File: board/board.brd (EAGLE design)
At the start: 49.6 x 37.9 mm, 17 parts

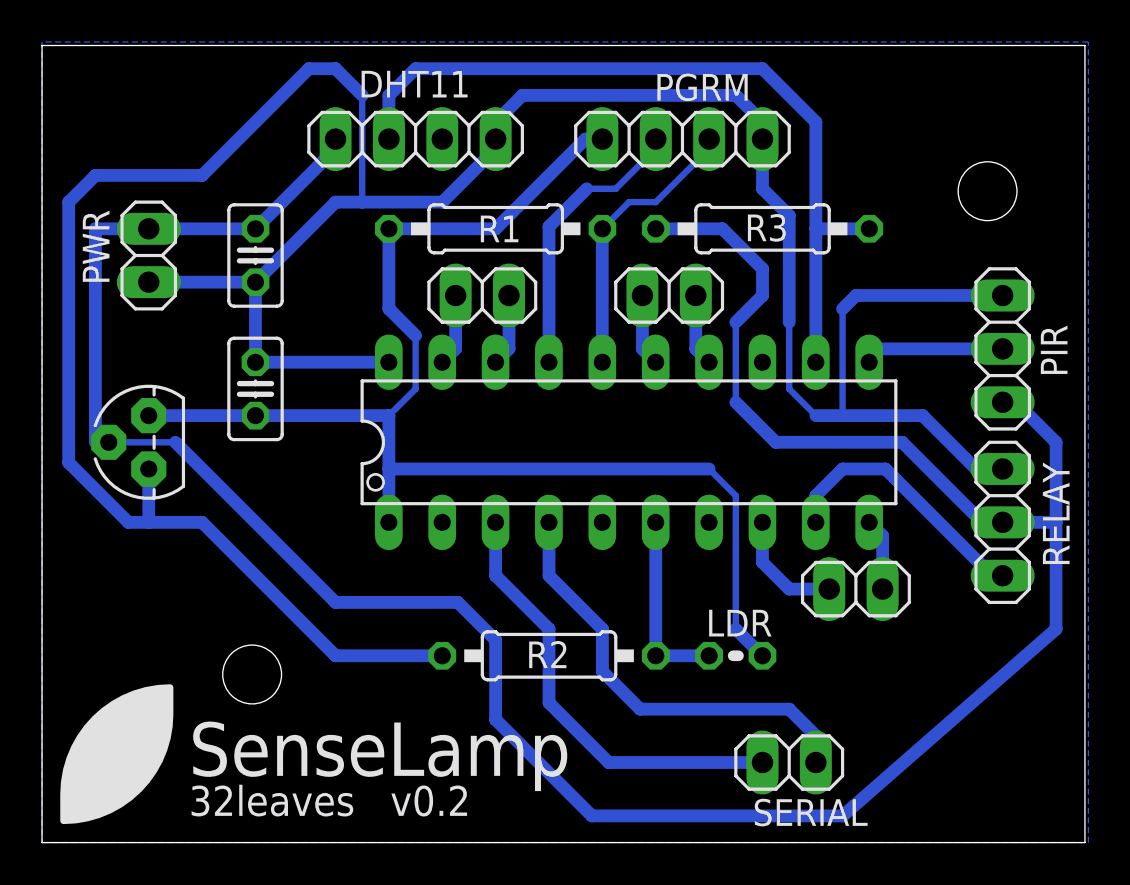
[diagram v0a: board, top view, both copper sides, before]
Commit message: fixed some space issues of the v0.1 board
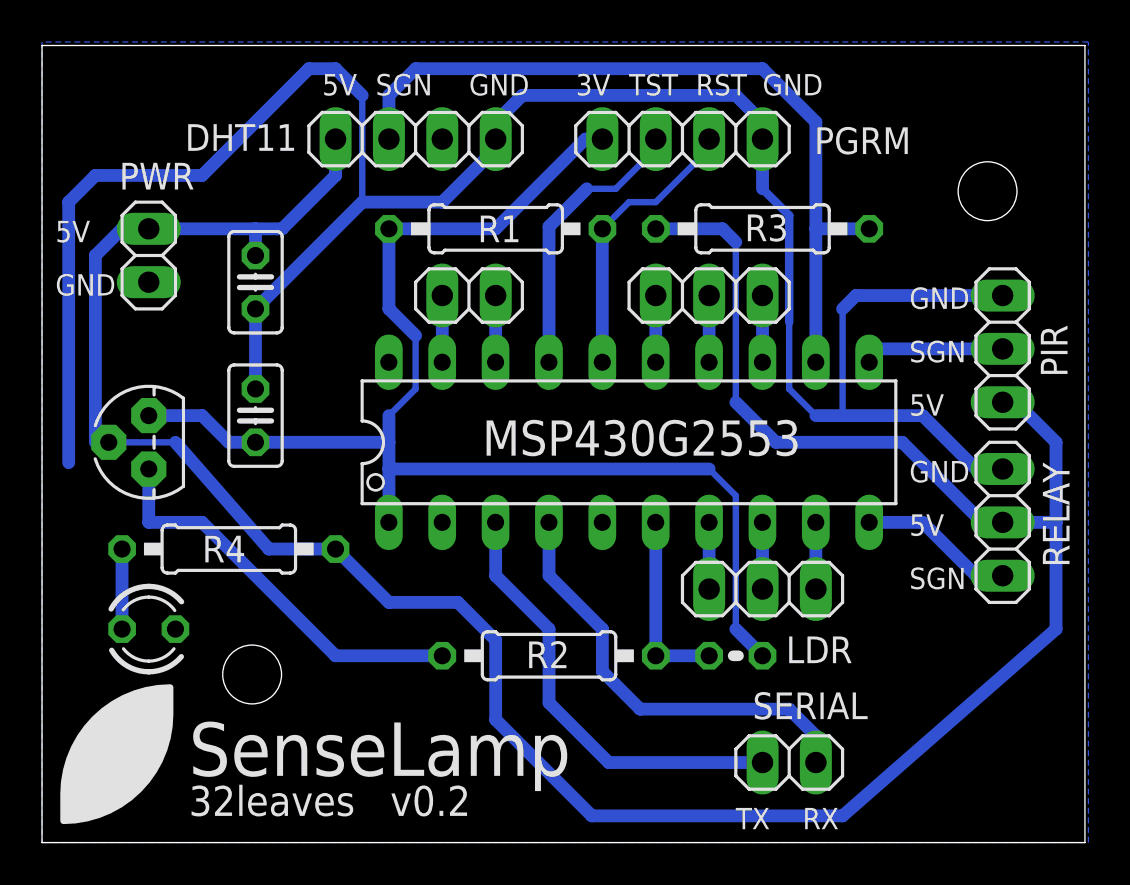
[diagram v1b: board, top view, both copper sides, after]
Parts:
- added LED1: (no value), led:LED3MM
- added R4: 47, rcl:0207/10
- IO0, IO3: device pinhead:1X02 -> pinhead:1X03
- moved IO3 4.45 mm to (34.3, 12.1)
- moved IO0 1.91 mm to (31.8, 26.0)
- moved C1 1.27 mm to (10.2, 26.7)
- moved C2 1.27 mm to (10.2, 20.3)
- moved IO2 0.63 mm to (20.3, 26.0)
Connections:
- removed net IO2.2: IO3.2, U$1.10
- new net IO1.5: IO3.1, U$1.7
- new net IO2.1: IO3.3, U$1.9
- new net IO2.5: IO0.3, U$1.13
- new net N$1: LED1.A, R4.1
- net GND: now also LED1.K
- net IO2.0: now also IO3.2; no longer IO3.1
- net REL: now also U$1.10; no longer U$1.9
- net VCC_5V: now also R4.2
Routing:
- net GND: track 142.0 -> 126.1 mm
- net REL: track 12.8 -> 7.41 mm
- net N$1: track 0.00 -> 3.81 mm
- net IO2.2: track 3.44 -> 0.00 mm
- net IO2.5: track 0.00 -> 3.18 mm
- net IO1.5: track 0.00 -> 3.18 mm
- net IO2.1: track 0.00 -> 3.18 mm
- net IO2.0: track 5.61 -> 3.18 mm
- net VCC_5V: track 124.8 -> 125.7 mm
- net VCC: track 63.6 -> 64.1 mm
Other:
- board text added: "3V"
- board text added: "5V"
- board text added: "GND"
- board text added: "MSP430G2553"
- board text added: "RST"
- board text added: "RX"
- board text added: "SGN"
- board text added: "TST"
- board text added: "TX"

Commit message: finished the v02 board
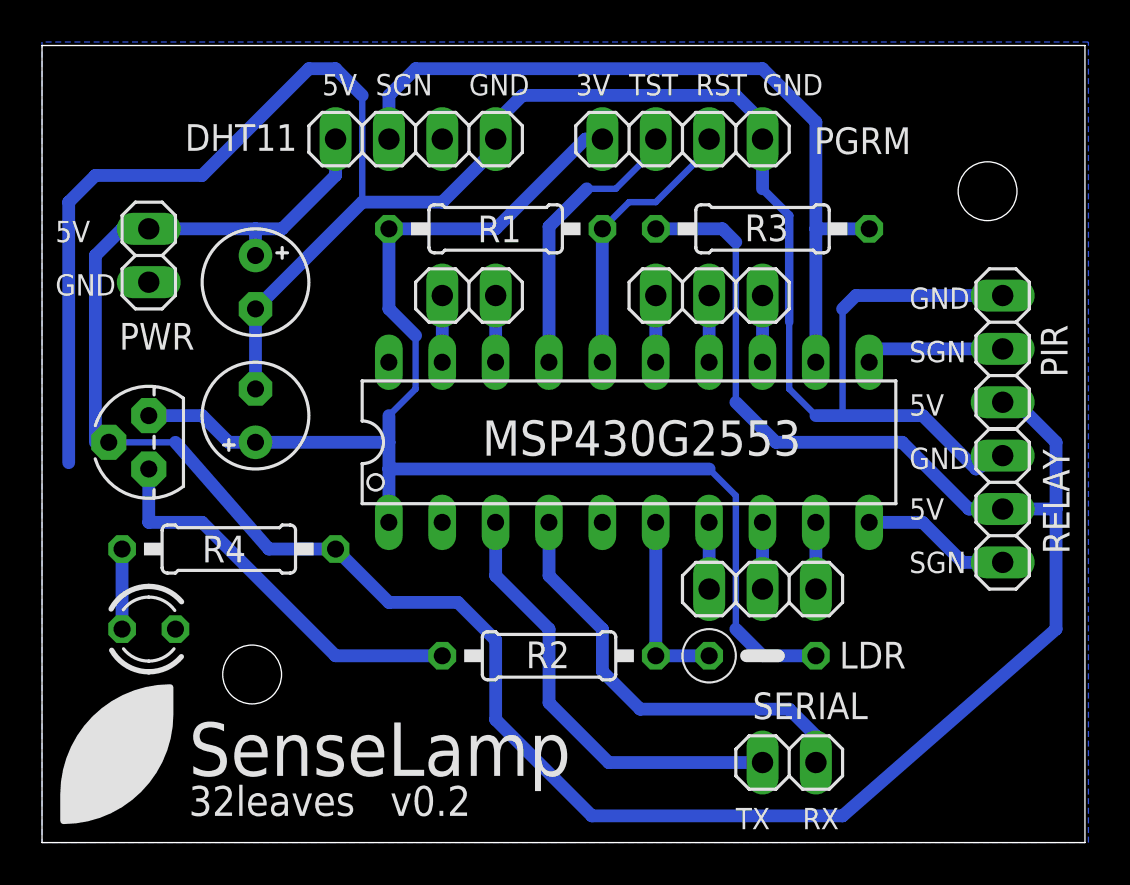
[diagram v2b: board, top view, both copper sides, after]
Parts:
- C1, C2: device rcl:C025-025X050 -> rcl:E2,5-5
- LDR: device rcl:0204V -> rcl:0207/5V
- moved LDR 1.27 mm to (34.3, 8.89)
- moved RELAY 0.63 mm to (45.7, 15.9)
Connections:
- net GND: now also C1.-, C2.-; no longer C1.2, C2.2
- net VCC: now also C2.+; no longer C2.1
- net VCC_5V: now also C1.+; no longer C1.1
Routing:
- net VCC: track 64.1 -> 66.6 mm
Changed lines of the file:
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@@
 <text x="0.635" y="26.035" size="1.016" layer="21" font="vector" ratio="9">GND</text>
 <text x="41.275" y="25.4" size="1.016" layer="21" font="vector" ratio="9">GND</text>
-<text x="41.275" y="17.145" size="1.016" layer="21" font="vector" ratio="9">GND</text>
+<text x="41.275" y="17.78" size="1.016" layer="21" font="vector" ratio="9">GND</text>
 <text x="20.32" y="35.56" size="1.016" layer="21" font="vector" ratio="9">GND</text>
 <text x="34.29" y="35.56" size="1.016" layer="21" font="vector" ratio="9">GND</text>
@@
 <text x="13.335" y="35.56" size="1.016" layer="21" font="vector" ratio="9">5V</text>
 <text x="41.275" y="20.32" size="1.016" layer="21" font="vector" ratio="9">5V</text>
-<text x="41.275" y="14.605" size="1.016" layer="21" font="vector" ratio="9">5V</text>
-<text x="41.275" y="12.065" size="1.016" layer="21" font="vector" ratio="9">SGN</text>
+<text x="41.275" y="15.367" size="1.016" layer="21" font="vector" ratio="9">5V</text>
+<text x="41.275" y="12.827" size="1.016" layer="21" font="vector" ratio="9">SGN</text>
 <text x="41.275" y="22.86" size="1.016" layer="21" font="vector" ratio="9">SGN</text>
 <text x="15.875" y="35.56" size="1.016" layer="21" font="vector" ratio="9">SGN</text>
@@
 <attribute name="VALUE" x="21.8694" y="8.255" size="1.27" layer="27" ratio="10"/>
 </element>
-<element name="LDR" library="rcl" package="0204V" value="" x="33.02" y="8.89" smashed="yes">
-<attribute name="NAME" x="35.40438125" y="8.538246875" size="1.27" layer="25" font="vector" ratio="10"/>
-<attribute name="VALUE" x="30.8864" y="6.5786" size="1.27" layer="27" ratio="10"/>
+<element name="LDR" library="rcl" package="0207/5V" value="" x="34.29" y="8.89" smashed="yes">
+<attribute name="NAME" x="37.94438125" y="8.284246875" size="1.27" layer="25" font="vector" ratio="10"/>
+<attribute name="VALUE" x="32.1564" y="6.5786" size="1.27" layer="27" ratio="10"/>
 </element>
 <element name="IC1" library="adafruit" package="TO92" value="" x="5.08" y="19.05" smashed="yes" rot="R90">
@@
 </element>
 <element name="PWR" library="pinhead" package="1X02" value="" x="5.08" y="27.94" smashed="yes" rot="R90">
-<attribute name="NAME" x="3.67286875" y="31.080446875" size="1.27" layer="25" font="vector" ratio="10"/>
+<attribute name="NAME" x="3.67286875" y="23.460446875" size="1.27" layer="25" font="vector" ratio="10"/>
 <attribute name="VALUE" x="8.255" y="25.4" size="1.27" layer="27" rot="R90"/>
 </element>
@@
 <attribute name="VALUE" x="32.0294" y="28.575" size="1.27" layer="27" ratio="10"/>
 </element>
-<element name="RELAY" library="pinhead" package="1X03" value="" x="45.72" y="15.24" smashed="yes" rot="R270">
-<attribute name="NAME" x="47.63209375" y="18.0839" size="1.27" layer="25" font="vector" ratio="10" rot="R270"/>
-<attribute name="VALUE" x="42.545" y="19.05" size="1.27" layer="27" rot="R270"/>
+<element name="RELAY" library="pinhead" package="1X03" value="" x="45.72" y="15.875" smashed="yes" rot="R270">
+<attribute name="NAME" x="47.63209375" y="18.7189" size="1.27" layer="25" font="vector" ratio="10" rot="R270"/>
+<attribute name="VALUE" x="42.545" y="19.685" size="1.27" layer="27" rot="R270"/>
 </element>
 <element name="PGRM" library="pinhead" package="1X04" value="" x="30.48" y="33.48" smashed="yes">
@@
 <attribute name="VALUE" x="25.4" y="30.305" size="1.27" layer="27"/>
 </element>
-<element name="C1" library="rcl" package="C025-025X050" value="10u" x="10.16" y="26.67" smashed="yes" rot="R270">
+<element name="C1" library="rcl" package="E2,5-5" value="10u" x="10.16" y="26.67" smashed="yes" rot="R270">
 <attribute name="VALUE" x="7.366" y="28.956" size="1.27" layer="27" ratio="10" rot="R270"/>
 </element>
-<element name="C2" library="rcl" package="C025-025X050" value="10u" x="10.16" y="20.32" smashed="yes" rot="R90">
+<element name="C2" library="rcl" package="E2,5-5" value="10u" x="10.16" y="20.32" smashed="yes" rot="R90">
 <attribute name="VALUE" x="12.954" y="18.034" size="1.27" layer="27" ratio="10" rot="R90"/>
 </element>
@@
 <contactref element="IC1" pad="1"/>
 <contactref element="PWR" pad="1"/>
-<contactref element="C2" pad="2"/>
-<contactref element="C1" pad="2"/>
+<contactref element="C2" pad="-"/>
+<contactref element="C1" pad="-"/>
 <contactref element="DHT11" pad="1"/>
 <contactref element="RELAY" pad="1"/>
@@
 <wire x1="13.97" y1="36.83" x2="15.24" y2="35.56" width="0.6096" layer="16"/>
 <wire x1="15.24" y1="35.56" x2="15.24" y2="30.48" width="0.3048" layer="16"/>
-<wire x1="45.72" y1="17.78" x2="44.45" y2="17.78" width="0.6096" layer="16"/>
+<wire x1="45.72" y1="18.415" x2="44.45" y2="17.78" width="0.6096" layer="16"/>
 <wire x1="44.45" y1="17.78" x2="41.91" y2="20.32" width="0.6096" layer="16"/>
 <wire x1="41.91" y1="20.32" x2="38.1" y2="20.32" width="0.6096" layer="16"/>
@@
 <contactref element="LDR" pad="2"/>
 <contactref element="IC1" pad="3"/>
-<contactref element="C2" pad="1"/>
+<contactref element="C2" pad="+"/>
 <wire x1="16.51" y1="15.24" x2="16.505" y2="15.24" width="0.254" layer="16"/>
 <wire x1="16.51" y1="17.78" x2="16.51" y2="15.24" width="0.6096" layer="16"/>
@@
 <wire x1="21.59" y1="29.21" x2="25.86" y2="33.48" width="0.6096" layer="16"/>
 <wire x1="25.86" y1="33.48" x2="26.67" y2="33.48" width="0.6096" layer="16"/>
+<wire x1="36.83" y1="8.89" x2="34.29" y2="8.89" width="0.6096" layer="16"/>
 <wire x1="34.29" y1="8.89" x2="33.02" y2="10.16" width="0.6096" layer="16"/>
 <wire x1="33.02" y1="10.16" x2="33.02" y2="16.51" width="0.3048" layer="16"/>
@@
 <contactref element="PWR" pad="2"/>
 <contactref element="IC1" pad="2"/>
-<contactref element="C1" pad="1"/>
+<contactref element="C1" pad="+"/>
 <contactref element="DHT11" pad="4"/>
 <contactref element="R3" pad="1"/>
@@
 <wire x1="19.79395" y1="11.43" x2="16.51" y2="11.43" width="0.6096" layer="16"/>
 <wire x1="6.35" y1="19.05" x2="3.175" y2="19.05" width="0.3048" layer="16"/>
-<wire x1="48.26" y1="10.16" x2="48.26" y2="15.24" width="0.6096" layer="16"/>
-<wire x1="48.26" y1="15.24" x2="45.72" y2="15.24" width="0.6096" layer="16"/>
+<wire x1="48.26" y1="10.16" x2="48.26" y2="15.875" width="0.6096" layer="16"/>
+<wire x1="48.26" y1="15.875" x2="45.72" y2="15.875" width="0.6096" layer="16"/>
 <wire x1="2.54" y1="19.05" x2="2.54" y2="27.94" width="0.6096" layer="16"/>
 <wire x1="2.54" y1="27.94" x2="3.81" y2="29.21" width="0.6096" layer="16"/>
@@
 <wire x1="32.385" y1="29.21" x2="29.21" y2="29.21" width="0.6096" layer="16"/>
 <contactref element="PIR" pad="1"/>
-<wire x1="40.93980625" y1="19.05" x2="44.74980625" y2="15.24" width="0.6096" layer="16"/>
-<wire x1="44.74980625" y1="15.24" x2="45.72" y2="15.24" width="0.6096" layer="16"/>
+<wire x1="40.93980625" y1="19.05" x2="44.11480625" y2="15.875" width="0.6096" layer="16"/>
+<wire x1="44.11480625" y1="15.875" x2="45.72" y2="15.875" width="0.6096" layer="16"/>
 <wire x1="45.72" y1="20.955" x2="46.355" y2="20.955" width="0.6096" layer="16"/>
 <wire x1="46.355" y1="20.955" x2="48.26" y2="19.05" width="0.6096" layer="16"/>
-<wire x1="48.26" y1="19.05" x2="48.26" y2="15.24" width="0.6096" layer="16"/>
+<wire x1="48.26" y1="19.05" x2="48.26" y2="15.875" width="0.6096" layer="16"/>
 <wire x1="5.08" y1="29.21" x2="10.16" y2="29.21" width="0.6096" layer="16"/>
 <wire x1="10.16" y1="27.94" x2="10.16" y2="29.21" width="0.6096" layer="16"/>
@@
 <contactref element="U$1" pad="10"/>
 <wire x1="39.365" y1="15.24" x2="41.91" y2="15.24" width="0.6096" layer="16"/>
-<wire x1="41.91" y1="15.24" x2="44.45" y2="12.7" width="0.6096" layer="16"/>
-<wire x1="44.45" y1="12.7" x2="45.72" y2="12.7" width="0.6096" layer="16"/>
+<wire x1="41.91" y1="15.24" x2="43.815" y2="13.335" width="0.6096" layer="16"/>
+<wire x1="43.815" y1="13.335" x2="45.72" y2="13.335" width="0.6096" layer="16"/>
 </signal>
 <signal name="TEST">

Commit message: updated the board and firmware to a new revision / pin mapping is now correct and installing a PIR sensor is a lot easier
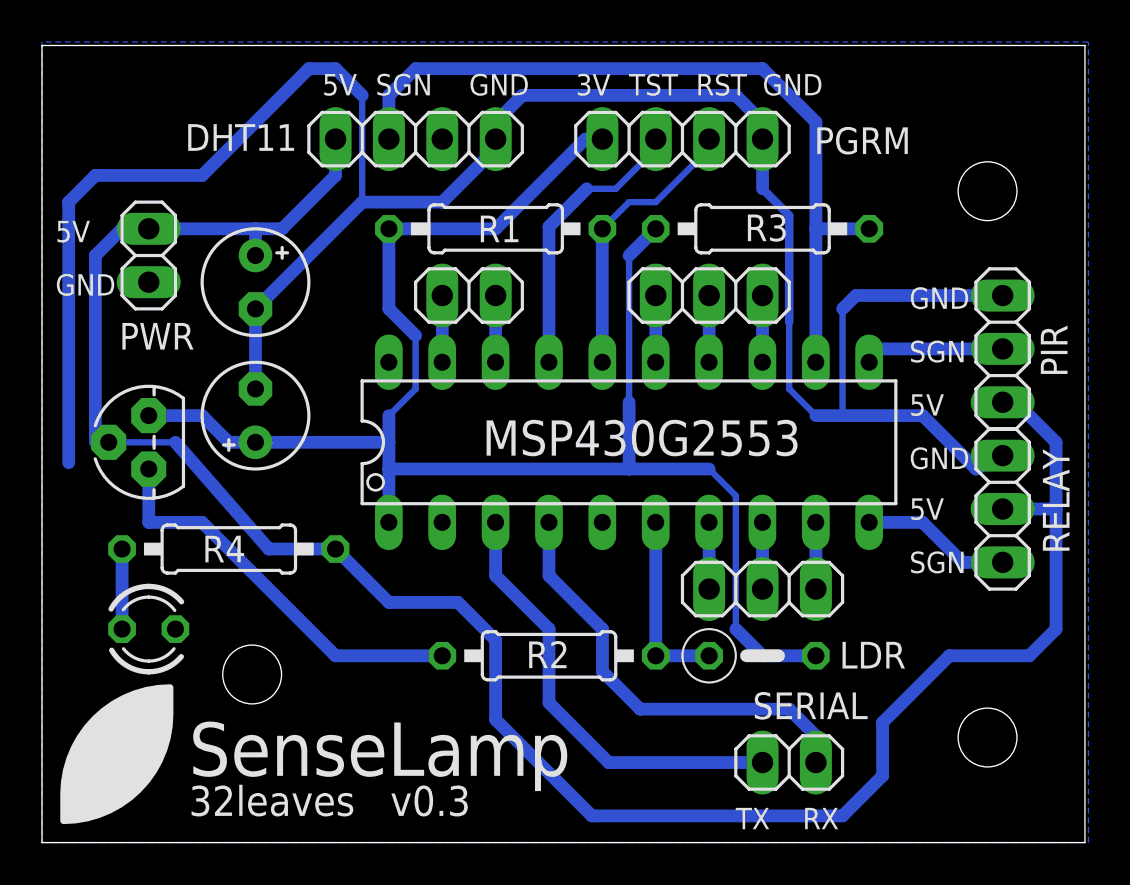
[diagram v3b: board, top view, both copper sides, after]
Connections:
- net VCC: now also R3.1
- net VCC_5V: no longer R3.1
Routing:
- net VCC_5V: track 125.5 -> 100.3 mm
- net VCC: track 66.6 -> 78.6 mm
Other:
- board text added: "32leaves v0.3"
- board text removed: "32leaves v0.2"
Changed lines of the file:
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@@
 <layer number="43" name="vRestrict" color="2" fill="10" visible="no" active="yes"/>
 <layer number="44" name="Drills" color="7" fill="1" visible="no" active="yes"/>
-<layer number="45" name="Holes" color="7" fill="1" visible="no" active="yes"/>
+<layer number="45" name="Holes" color="7" fill="1" visible="yes" active="yes"/>
 <layer number="46" name="Milling" color="3" fill="1" visible="no" active="yes"/>
 <layer number="47" name="Measures" color="7" fill="1" visible="no" active="yes"/>
@@
 <hole x="45" y="31" drill="2.8"/>
 <text x="6.985" y="3.175" size="2.54" layer="21" font="vector">SenseLamp</text>
-<text x="6.985" y="1.27" size="1.4224" layer="21" font="vector">32leaves   v0.2</text>
+<text x="6.985" y="1.27" size="1.4224" layer="21" font="vector">32leaves   v0.3</text>
 <polygon width="0.3048" layer="21">
 <vertex x="1.020121875" y="1.032653125"/>
@@
 <text x="36.195" y="0.635" size="1.016" layer="21" font="vector" ratio="9">RX</text>
 <text x="20.955" y="18.415" size="1.6764" layer="21" font="vector" ratio="9">MSP430G2553</text>
+<hole x="45" y="5" drill="2.8"/>
 </plain>
 <attributes>
@@
 <wire x1="33.02" y1="10.16" x2="33.02" y2="16.51" width="0.3048" layer="16"/>
 <wire x1="33.02" y1="16.51" x2="31.75" y2="17.78" width="0.3048" layer="16"/>
-<wire x1="31.75" y1="17.78" x2="16.51" y2="17.78" width="0.6096" layer="16"/>
+<wire x1="31.75" y1="17.78" x2="27.94" y2="17.78" width="0.6096" layer="16"/>
+<wire x1="27.94" y1="17.78" x2="16.51" y2="17.78" width="0.6096" layer="16"/>
 <wire x1="16.51" y1="17.78" x2="16.51" y2="19.05" width="0.6096" layer="16"/>
 <wire x1="16.51" y1="20.32" x2="16.51" y2="19.05" width="0.6096" layer="16"/>
@@
 <wire x1="8.89" y1="19.05" x2="7.62" y2="20.32" width="0.6096" layer="16"/>
 <wire x1="7.62" y1="20.32" x2="5.08" y2="20.32" width="0.6096" layer="16"/>
+<contactref element="R3" pad="1"/>
+<wire x1="29.21" y1="29.21" x2="27.94" y2="27.94" width="0.6096" layer="16"/>
+<wire x1="27.94" y1="27.94" x2="27.94" y2="20.955" width="0.3048" layer="16"/>
+<wire x1="27.94" y1="20.955" x2="27.94" y2="17.78" width="0.6096" layer="16"/>
 </signal>
 <signal name="N$2">
@@
 <contactref element="IC1" pad="2"/>
 <contactref element="C1" pad="+"/>
-<contactref element="DHT11" pad="4"/>
-<contactref element="R3" pad="1"/>
 <contactref element="RELAY" pad="2"/>
 <wire x1="2.54" y1="19.05" x2="3.175" y2="19.05" width="0.3048" layer="16"/>
@@
 <wire x1="2.54" y1="27.94" x2="3.81" y2="29.21" width="0.6096" layer="16"/>
 <wire x1="3.81" y1="29.21" x2="5.08" y2="29.21" width="0.6096" layer="16"/>
-<wire x1="38.1" y1="1.27" x2="48.26" y2="10.16" width="0.6096" layer="16"/>
-<wire x1="13.97" y1="33.02" x2="13.97" y2="33.48" width="0.6096" layer="16"/>
-<wire x1="34.925" y1="19.05" x2="40.93980625" y2="19.05" width="0.6096" layer="16"/>
-<wire x1="34.925" y1="19.05" x2="33.02" y2="20.955" width="0.6096" layer="16"/>
-<wire x1="33.02" y1="20.955" x2="33.02" y2="28.575" width="0.3048" layer="16"/>
-<wire x1="33.02" y1="28.575" x2="32.385" y2="29.21" width="0.6096" layer="16"/>
-<wire x1="32.385" y1="29.21" x2="29.21" y2="29.21" width="0.6096" layer="16"/>
 <contactref element="PIR" pad="1"/>
-<wire x1="40.93980625" y1="19.05" x2="44.11480625" y2="15.875" width="0.6096" layer="16"/>
-<wire x1="44.11480625" y1="15.875" x2="45.72" y2="15.875" width="0.6096" layer="16"/>
 <wire x1="45.72" y1="20.955" x2="46.355" y2="20.955" width="0.6096" layer="16"/>
 <wire x1="46.355" y1="20.955" x2="48.26" y2="19.05" width="0.6096" layer="16"/>
@@
 <wire x1="10.16" y1="29.21" x2="11.43" y2="29.21" width="0.6096" layer="16"/>
 <wire x1="11.43" y1="29.21" x2="13.97" y2="31.75" width="0.6096" layer="16"/>
-<wire x1="13.97" y1="31.75" x2="13.97" y2="33.48" width="0.6096" layer="16"/>
 <contactref element="R4" pad="2"/>
 <wire x1="13.97" y1="13.97" x2="16.51" y2="11.43" width="0.6096" layer="16"/>
 <wire x1="6.35" y1="19.05" x2="10.795" y2="13.97" width="0.6096" layer="16"/>
 <wire x1="10.795" y1="13.97" x2="13.97" y2="13.97" width="0.6096" layer="16"/>
+<contactref element="DHT11" pad="4"/>
+<wire x1="13.97" y1="31.75" x2="13.97" y2="33.48" width="0.6096" layer="16"/>
+<wire x1="38.1" y1="1.27" x2="40.005" y2="3.175" width="0.6096" layer="16"/>
+<wire x1="40.005" y1="3.175" x2="40.005" y2="5.715" width="0.6096" layer="16"/>
+<wire x1="40.005" y1="5.715" x2="43.18" y2="8.89" width="0.6096" layer="16"/>
+<wire x1="43.18" y1="8.89" x2="46.99" y2="8.89" width="0.6096" layer="16"/>
+<wire x1="46.99" y1="8.89" x2="48.26" y2="10.16" width="0.6096" layer="16"/>
 </signal>
 <signal name="DHT">
